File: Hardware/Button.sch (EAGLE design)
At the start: 8 parts, among them Q1 IRLML5203, Q2 BC817-16LT1SMD, Q3 BC817-16LT1SMD

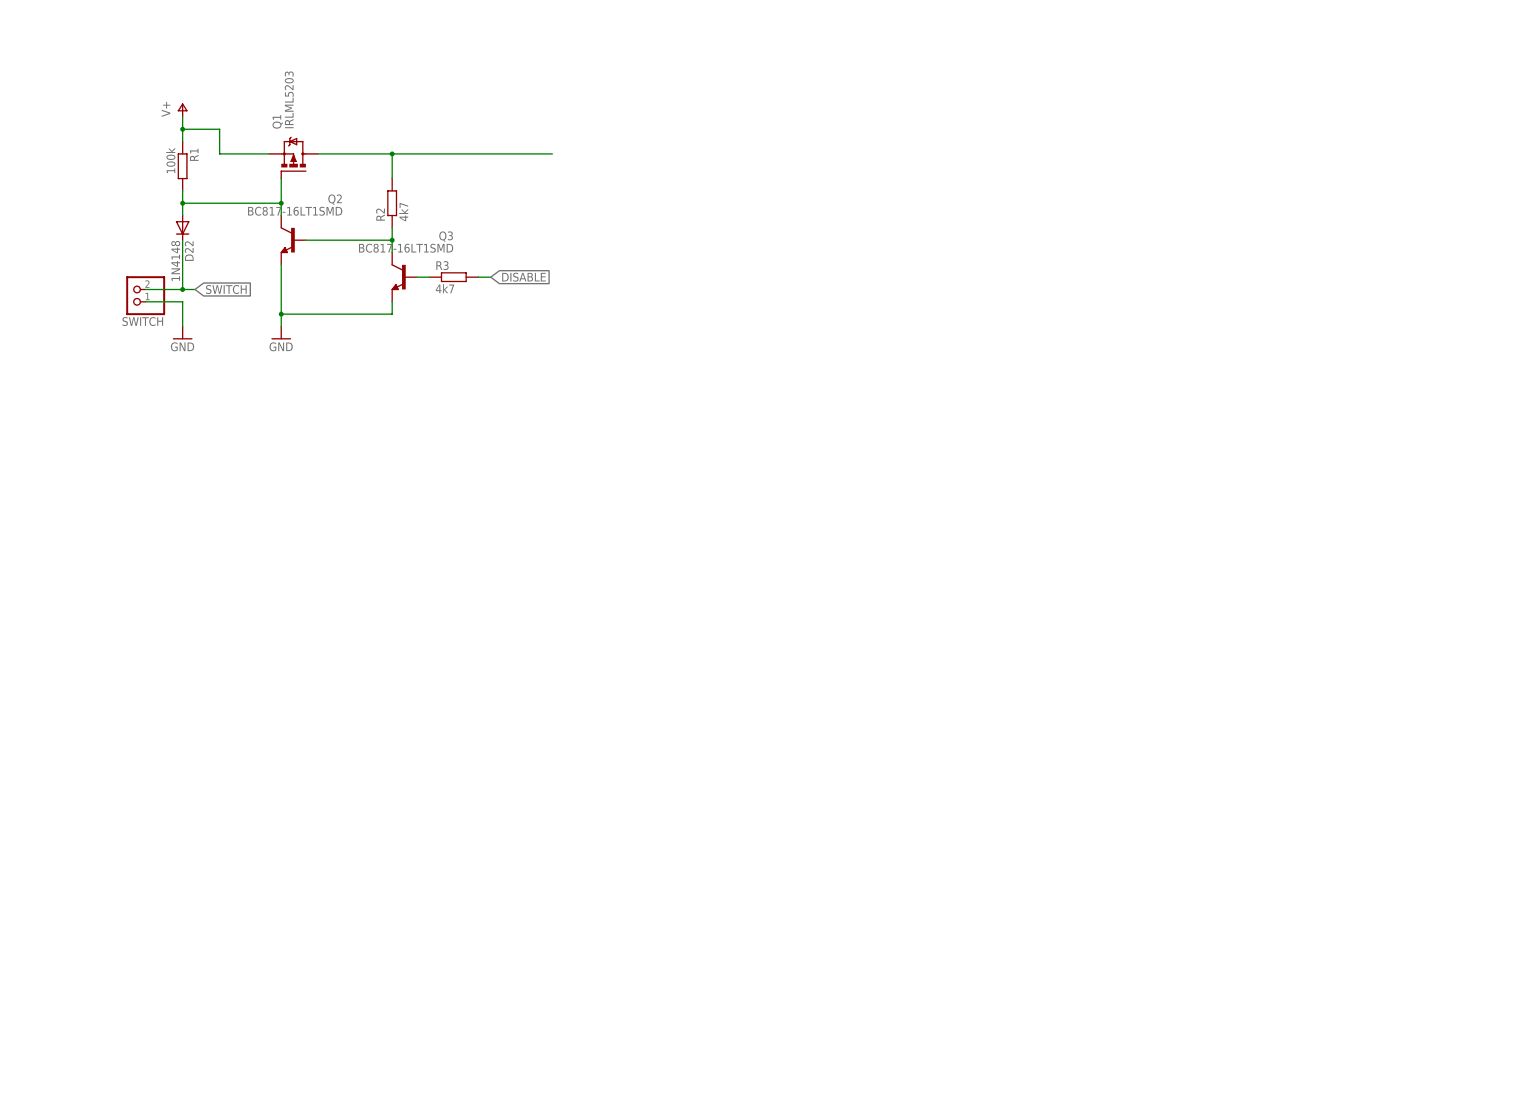
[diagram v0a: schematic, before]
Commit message: Added crystal to display board
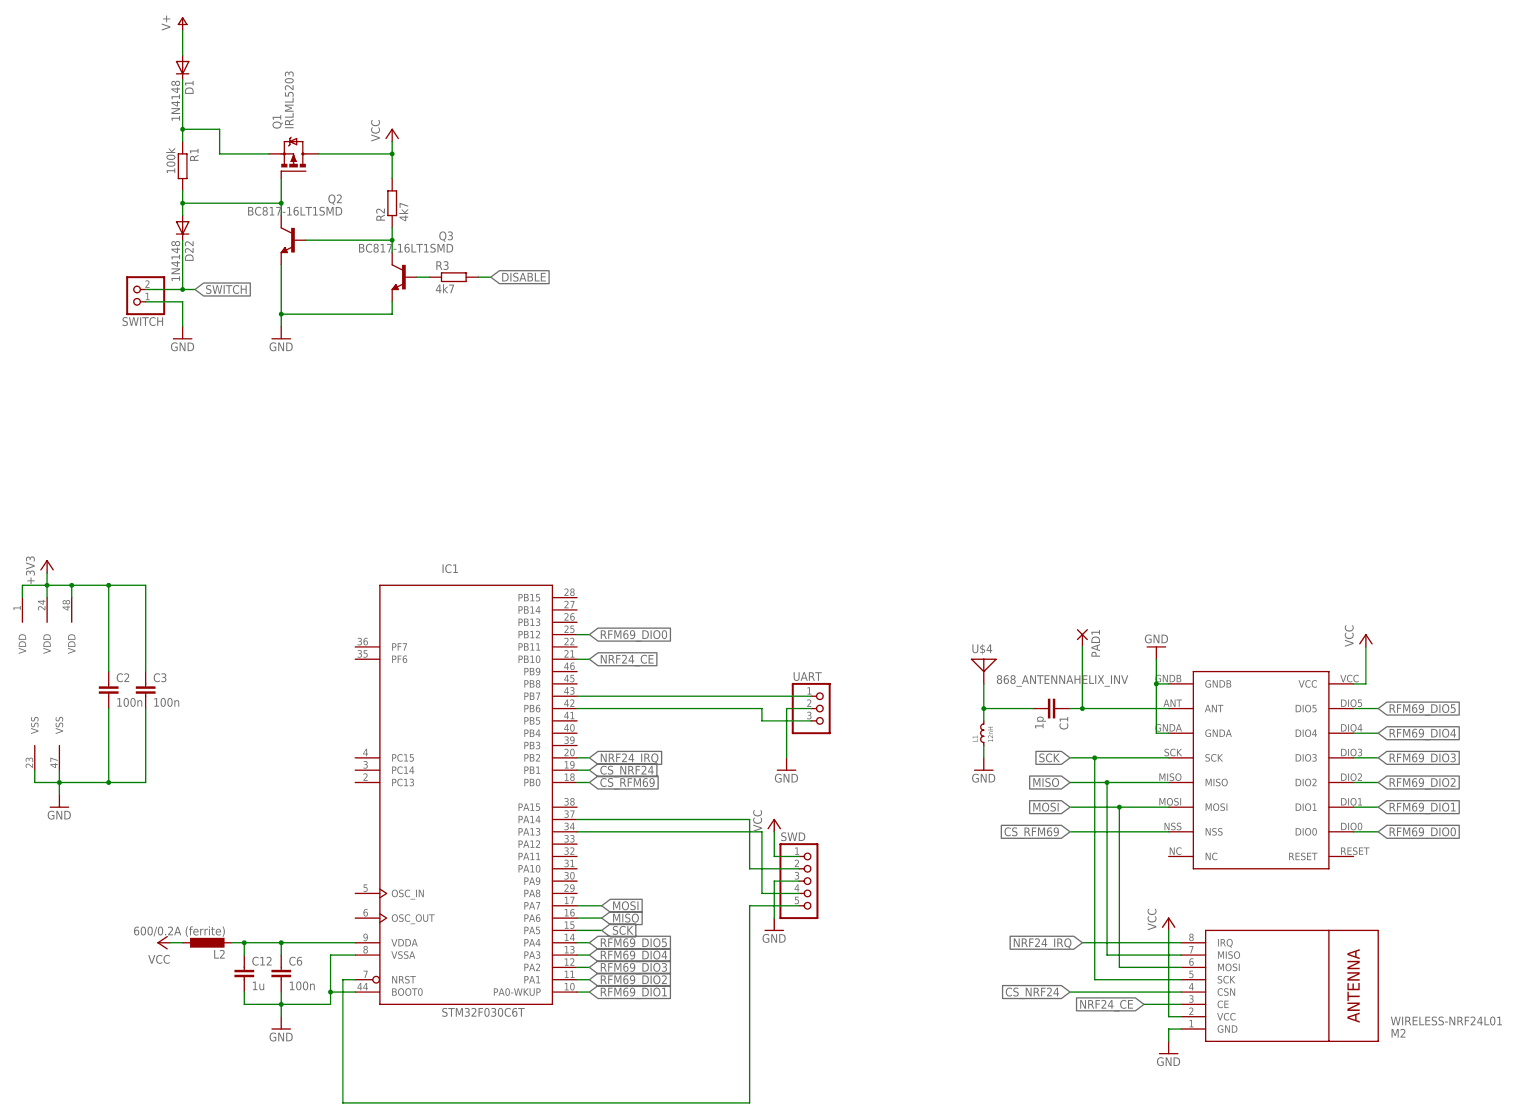
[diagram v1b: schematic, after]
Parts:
- added C1: 1p, rcl:C-EUC0603
- added C12: 1u, rcl:C-EUC0603
- added C2, C3: 100n, rcl:C-EUC0603K
- added C6: 100n, rcl:C-EUC0603
- added D1: 1N4148, diode:DIODE-SOD323-W
- added IC1: STM32F030C6T, micro-stm_v3:STM32F030C6T
- added L1: 12nH, standardparts:RF-INDUCTOR.0603
- added L2: 600/0.2A (ferrite), rcl:L-EUL2012C
- added M2: WIRELESS-NRF24L01, diy-modules:WIRELESS-NRF24L01
- added PAD1: (no value), wirepad:1,6/0,8
- added SWD: (no value), pinhead:PINHD-1X5
- added U$1: RFM69HW, hoperf:RFM69HW
- added U$4: 868_ANTENNAHELIX_INV, antenna:868_ANTENNAHELIX_INV
- added UART: (no value), pinhead:PINHD-1X3
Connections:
- removed net N$3: Q1.D, R2.2
- new net +3V3: C2.1, C3.1, IC1PWR.VDD@1, IC1PWR.VDD@2, IC1PWR.VDD@3
- new net CS_NRF24: IC1MCU.PB1, M2.CSN
- new net CS_RFM69: IC1MCU.PB0, U$1.NSS
- new net MISO: IC1MCU.PA6, M2.MISO, U$1.MISO
- new net MOSI: IC1MCU.PA7, M2.MOSI, U$1.MOSI
- new net N$4: C1.1, PAD1.P, U$1.ANT
- new net N$5: C1.2, L1.2, U$4.1
- new net N$6: D1.C, Q1.S, R1.1
- new net NRF24_CE: IC1MCU.PB10, M2.CE
- new net NRF24_IRQ: IC1MCU.PB2, M2.IRQ
- new net NRST: IC1MCU.NRST, SWD.5
- new net RFM69_DIO0: IC1MCU.PB12, U$1.DIO0
- new net RFM69_DIO1: IC1MCU.PA0-WKUP, U$1.DIO1
- new net RFM69_DIO2: IC1MCU.PA1, U$1.DIO2
- new net RFM69_DIO3: IC1MCU.PA2, U$1.DIO3
- new net RFM69_DIO4: IC1MCU.PA3, U$1.DIO4
- new net RFM69_DIO5: IC1MCU.PA4, U$1.DIO5
- new net RX: IC1MCU.PB7, UART.1
- new net SCK: IC1MCU.PA5, M2.SCK, U$1.SCK
- new net SWCLK: IC1MCU.PA14, SWD.2
- new net SWDIO: IC1MCU.PA13, SWD.4
- new net TX: IC1MCU.PB6, UART.3
- new net VCC: L2.1, M2.VCC, Q1.D, R2.2, SWD.1, U$1.VCC
- new net VDDA: C12.1, C6.1, IC1MCU.VDDA, L2.2
- net GND: now also C12.2, C2.2, C3.2, C6.2, IC1MCU.BOOT0, IC1MCU.VSSA, IC1PWR.VSS@1, IC1PWR.VSS@2, L1.1, M2.GND, SWD.3, U$1.GNDA, U$1.GNDB, UART.2
- net V+: now also D1.A; no longer Q1.S, R1.1

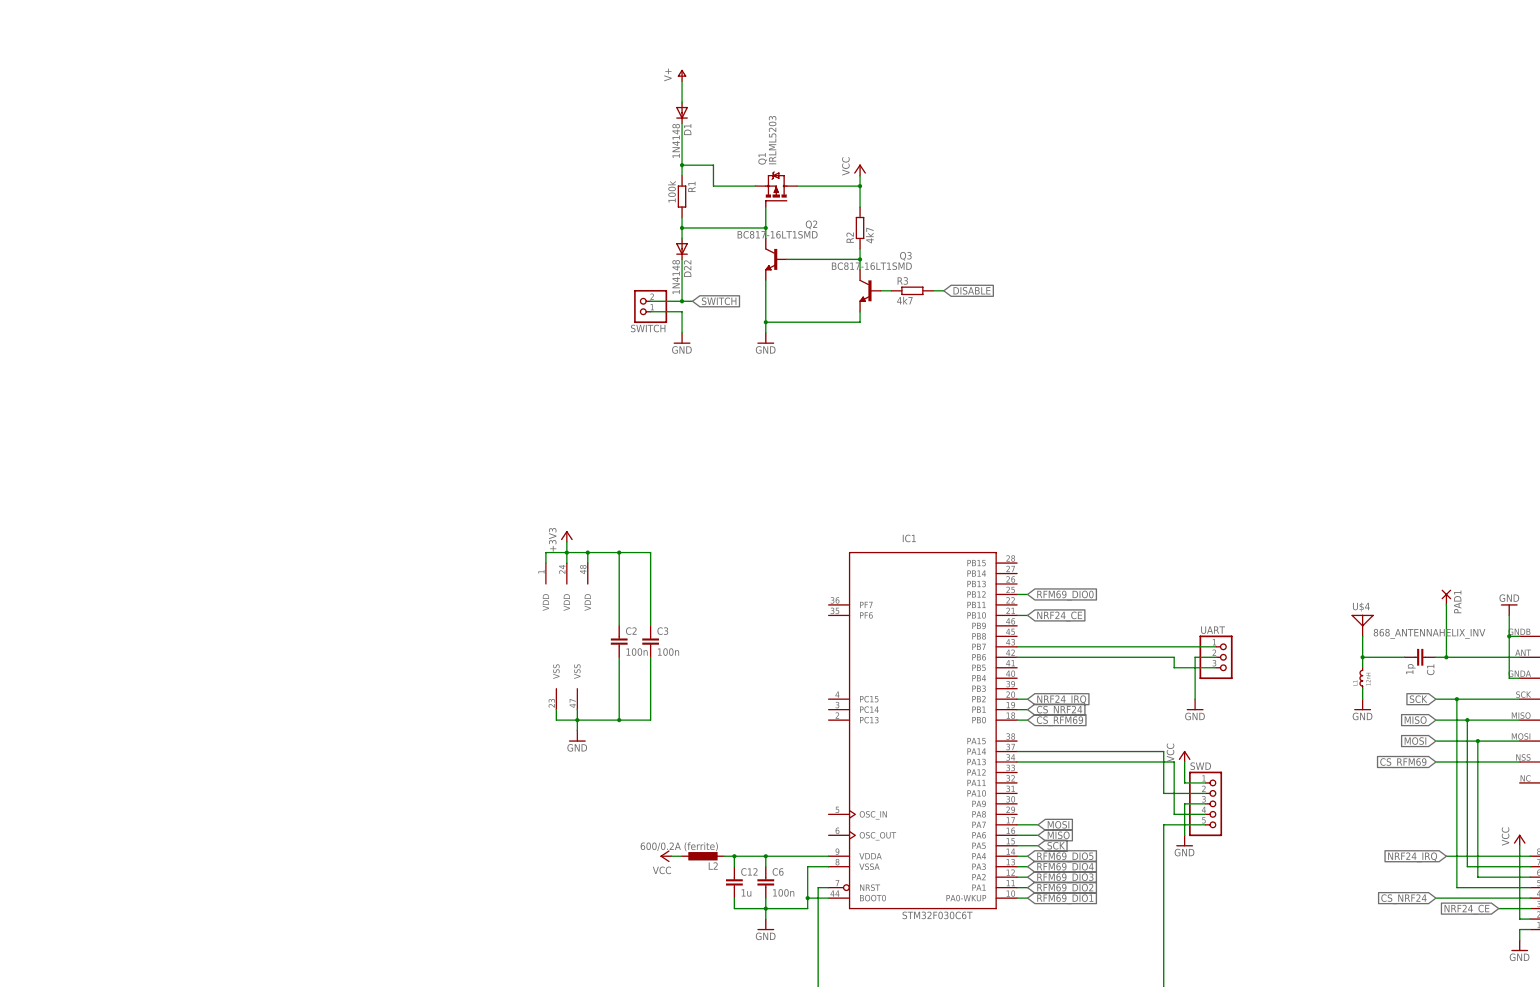
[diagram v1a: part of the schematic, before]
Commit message: Button Layout done
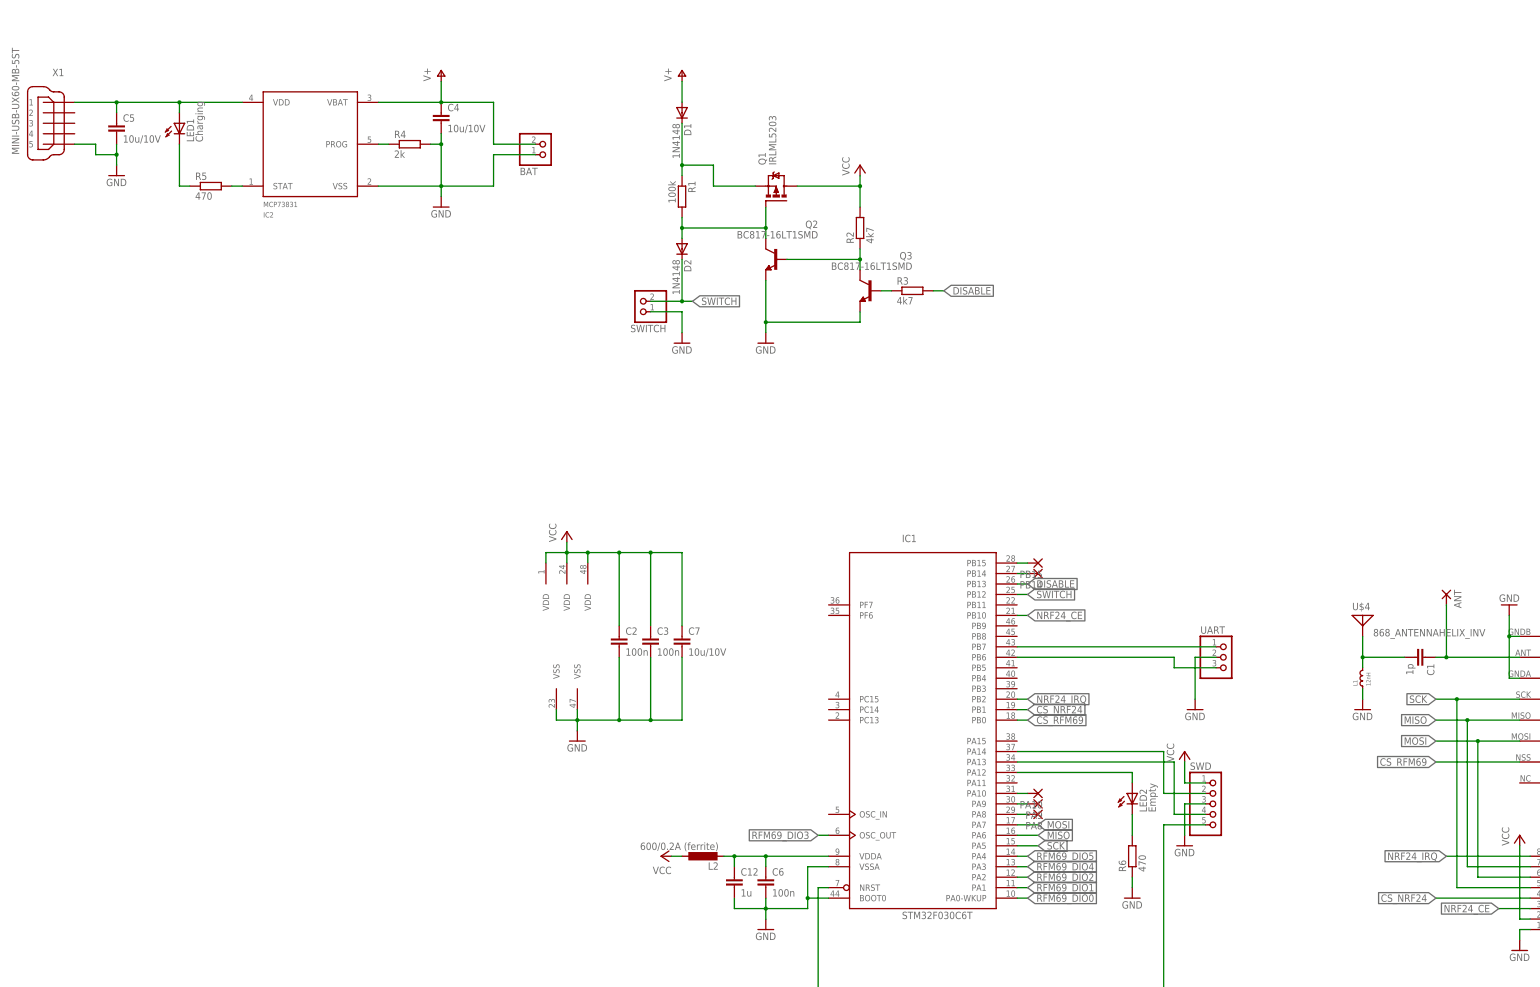
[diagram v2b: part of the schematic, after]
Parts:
- added BAT: (no value), pinhead:PINHD-1X2
- added C4, C5, C7: 10u/10V, rcl:C-EUC1206
- added IC2: MCP73831, mcp:MCP73831
- added LED1: Charging, led:LEDCHIPLED_0603
- added LED2: Empty, led:LEDCHIPLED_0603
- added PA10, PA8, PA9, PB14, PB15: (no value), wirepad:SMD2
- added R4: 2k, rcl:R-EU_R0603
- added R5, R6: 470, rcl:R-EU_R0603
- added X1: MINI-USB-UX60-MB-5ST, con-hirose:MINI-USB-UX60-MB-5ST
- C2, C3: device rcl:C-EUC0603K -> rcl:C-EUC0603
- renumbered D22 to D2, PAD1 to ANT
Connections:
- removed net +3V3: C2.1, C3.1, IC1PWR.VDD@1, IC1PWR.VDD@2, IC1PWR.VDD@3
- new net N$10: LED1.C, R5.1
- new net N$11: IC1MCU.PB15, PB15.P
- new net N$12: IC1MCU.PB14, PB14.P
- new net N$14: IC1MCU.PA10, PA10.P
- new net N$15: IC1MCU.PA9, PA9.P
- new net N$16: IC1MCU.PA8, PA8.P
- new net N$3: IC2.PROG, R4.1
- new net N$7: LED2.C, R6.2
- new net N$8: IC2.STAT, R5.2
- new net N$9: IC1MCU.PA12, LED2.A
- new net VIN: C5.1, IC2.VDD, LED1.A, X1.1
- net DISABLE: now also IC1MCU.PB13
- net GND: now also BAT.1, C4.2, C5.2, C7.2, IC2.VSS, R4.2, R6.1, X1.5
- net RFM69_DIO0: now also IC1MCU.PA0-WKUP; no longer IC1MCU.PB12
- net RFM69_DIO1: now also IC1MCU.PA1; no longer IC1MCU.PA0-WKUP
- net RFM69_DIO2: now also IC1MCU.PA2; no longer IC1MCU.PA1
- net RFM69_DIO3: now also IC1MCU.OSC_OUT; no longer IC1MCU.PA2
- net SWITCH: now also IC1MCU.PB12
- net V+: now also BAT.2, C4.1, IC2.VBAT
- net VCC: now also C2.1, C3.1, C7.1, IC1PWR.VDD@1, IC1PWR.VDD@2, IC1PWR.VDD@3
